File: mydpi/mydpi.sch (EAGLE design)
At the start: 16 parts, among them Q1 DMN3404L, U1 MEGA32U4-MU, U2 AP7381-33Y-13

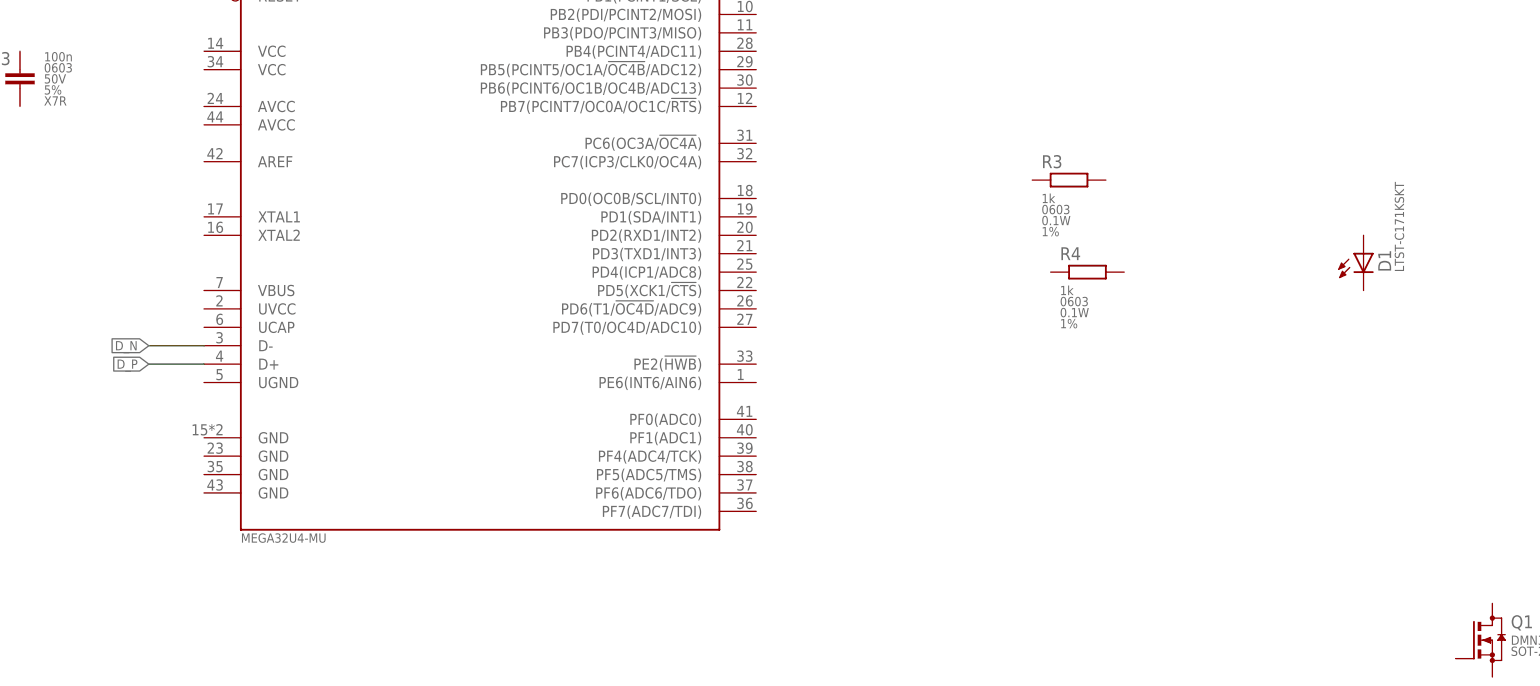
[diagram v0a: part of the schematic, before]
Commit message: Added supply voltage
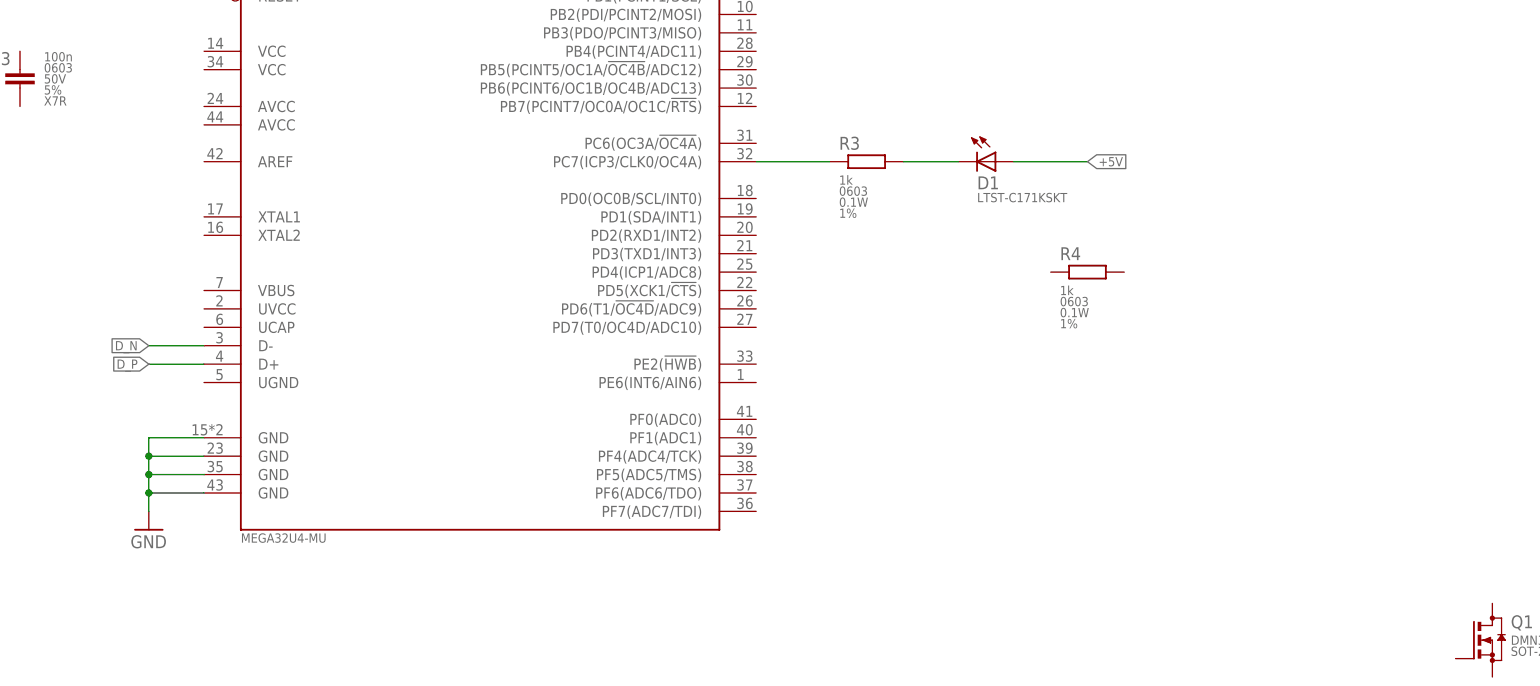
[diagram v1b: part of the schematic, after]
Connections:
- new net +5V: D1.A
- new net GND: U1.GND@1, U1.GND@2, U1.GND@3, U1.GND@4
- new net N$1: R3.1, U1.PC7(ICP3/CLK0/OC4A)
- new net N$2: D1.C, R3.2
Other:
- moved on the sheet: D1, R3
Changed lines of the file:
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@@
 <part name="Q1" library="zaan-Discrete" deviceset="DMN3404L" device="" package3d_urn="urn:adsk.eagle:package:28738/2"/>
 <part name="U2" library="zaan-IC-Power" deviceset="AP7381" device="-33Y-13"/>
+<part name="GND1" library="supply1" library_urn="urn:adsk.eagle:library:371" deviceset="GND" device=""/>
 </parts>
 <sheets>
@@
 <attribute name="DIELECTRIC" x="206.502" y="173.482" size="1.27" layer="96" align="center-left"/>
 </instance>
-<instance part="R3" gate="G$1" x="218.44" y="139.7" smashed="yes">
-<attribute name="NAME" x="214.63" y="142.24" size="1.778" layer="95" align="center-left"/>
-<attribute name="VALUE" x="214.63" y="137.16" size="1.27" layer="96" align="center-left"/>
-<attribute name="PACKAGE-IN" x="214.63" y="135.636" size="1.27" layer="96" align="center-left"/>
-<attribute name="POWER" x="214.63" y="134.112" size="1.27" layer="96" align="center-left"/>
-<attribute name="TOLERANCE" x="214.63" y="132.588" size="1.27" layer="96" align="center-left"/>
+<instance part="R3" gate="G$1" x="190.5" y="142.24" smashed="yes">
+<attribute name="NAME" x="186.69" y="144.78" size="1.778" layer="95" align="center-left"/>
+<attribute name="VALUE" x="186.69" y="139.7" size="1.27" layer="96" align="center-left"/>
+<attribute name="PACKAGE-IN" x="186.69" y="138.176" size="1.27" layer="96" align="center-left"/>
+<attribute name="POWER" x="186.69" y="136.652" size="1.27" layer="96" align="center-left"/>
+<attribute name="TOLERANCE" x="186.69" y="135.128" size="1.27" layer="96" align="center-left"/>
 </instance>
 <instance part="R4" gate="G$1" x="220.98" y="127" smashed="yes">
@@
 <attribute name="TOLERANCE" x="217.17" y="119.888" size="1.27" layer="96" align="center-left"/>
 </instance>
-<instance part="D1" gate="G$1" x="259.08" y="129.54" smashed="yes">
-<attribute name="NAME" x="262.89" y="127" size="1.778" layer="95" rot="R90"/>
-<attribute name="VALUE" x="264.668" y="127" size="1.27" layer="96" rot="R90"/>
+<instance part="D1" gate="G$1" x="208.28" y="142.24" smashed="yes" rot="R270">
+<attribute name="NAME" x="205.74" y="138.43" size="1.778" layer="95"/>
+<attribute name="VALUE" x="205.74" y="136.652" size="1.27" layer="96"/>
 </instance>
 <instance part="Q1" gate="G$1" x="276.86" y="76.2" smashed="yes">
@@
 <attribute name="NAME" x="289.56" y="102.108" size="1.778" layer="95"/>
 <attribute name="VALUE" x="299.72" y="91.694" size="1.27" layer="96"/>
+</instance>
+<instance part="GND1" gate="1" x="91.44" y="91.44" smashed="yes">
+<attribute name="VALUE" x="88.9" y="88.9" size="1.778" layer="96"/>
 </instance>
 </instances>
@@
 <wire x1="99.06" y1="114.3" x2="91.44" y2="114.3" width="0.1524" layer="91"/>
 <label x="91.44" y="114.3" size="1.27" layer="95" rot="R180" xref="yes"/>
+</segment>
+</net>
+<net name="GND" class="0">
+<segment>
+<pinref part="U1" gate="G$1" pin="GND@1"/>
+<wire x1="99.06" y1="104.14" x2="91.44" y2="104.14" width="0.1524" layer="91"/>
+<wire x1="91.44" y1="104.14" x2="91.44" y2="101.6" width="0.1524" layer="91"/>
+<pinref part="U1" gate="G$1" pin="GND@2"/>
+<wire x1="91.44" y1="101.6" x2="91.44" y2="99.06" width="0.1524" layer="91"/>
+<wire x1="91.44" y1="99.06" x2="91.44" y2="96.52" width="0.1524" layer="91"/>
+<wire x1="91.44" y1="96.52" x2="91.44" y2="93.98" width="0.1524" layer="91"/>
+<wire x1="99.06" y1="101.6" x2="91.44" y2="101.6" width="0.1524" layer="91"/>
+<junction x="91.44" y="101.6"/>
+<pinref part="U1" gate="G$1" pin="GND@3"/>
+<wire x1="99.06" y1="99.06" x2="91.44" y2="99.06" width="0.1524" layer="91"/>
+<junction x="91.44" y="99.06"/>
+<pinref part="U1" gate="G$1" pin="GND@4"/>
+<wire x1="99.06" y1="96.52" x2="91.44" y2="96.52" width="0.1524" layer="91"/>
+<junction x="91.44" y="96.52"/>
+<pinref part="GND1" gate="1" pin="GND"/>
+</segment>
+</net>
+<net name="N$1" class="0">
+<segment>
+<pinref part="U1" gate="G$1" pin="PC7(ICP3/CLK0/OC4A)"/>
+<wire x1="175.26" y1="142.24" x2="185.42" y2="142.24" width="0.1524" layer="91"/>
+<pinref part="R3" gate="G$1" pin="1"/>
+</segment>
+</net>
+<net name="N$2" class="0">
+<segment>
+<pinref part="R3" gate="G$1" pin="2"/>
+<pinref part="D1" gate="G$1" pin="C"/>
+<wire x1="195.58" y1="142.24" x2="203.2" y2="142.24" width="0.1524" layer="91"/>
+</segment>
+</net>
+<net name="+5V" class="0">
+<segment>
+<pinref part="D1" gate="G$1" pin="A"/>
+<wire x1="210.82" y1="142.24" x2="220.98" y2="142.24" width="0.1524" layer="91"/>
+<label x="220.98" y="142.24" size="1.27" layer="95" xref="yes"/>
 </segment>
 </net>
@@
 </drawing>
 <compatibility>
+<note version="8.2" severity="warning">
+Since Version 8.2, EAGLE supports online libraries. The ids
+of those online libraries will not be understood (or retained)
+with this version.
+</note>
 <note version="8.3" severity="warning">
 Since Version 8.3, EAGLE supports URNs for individual library

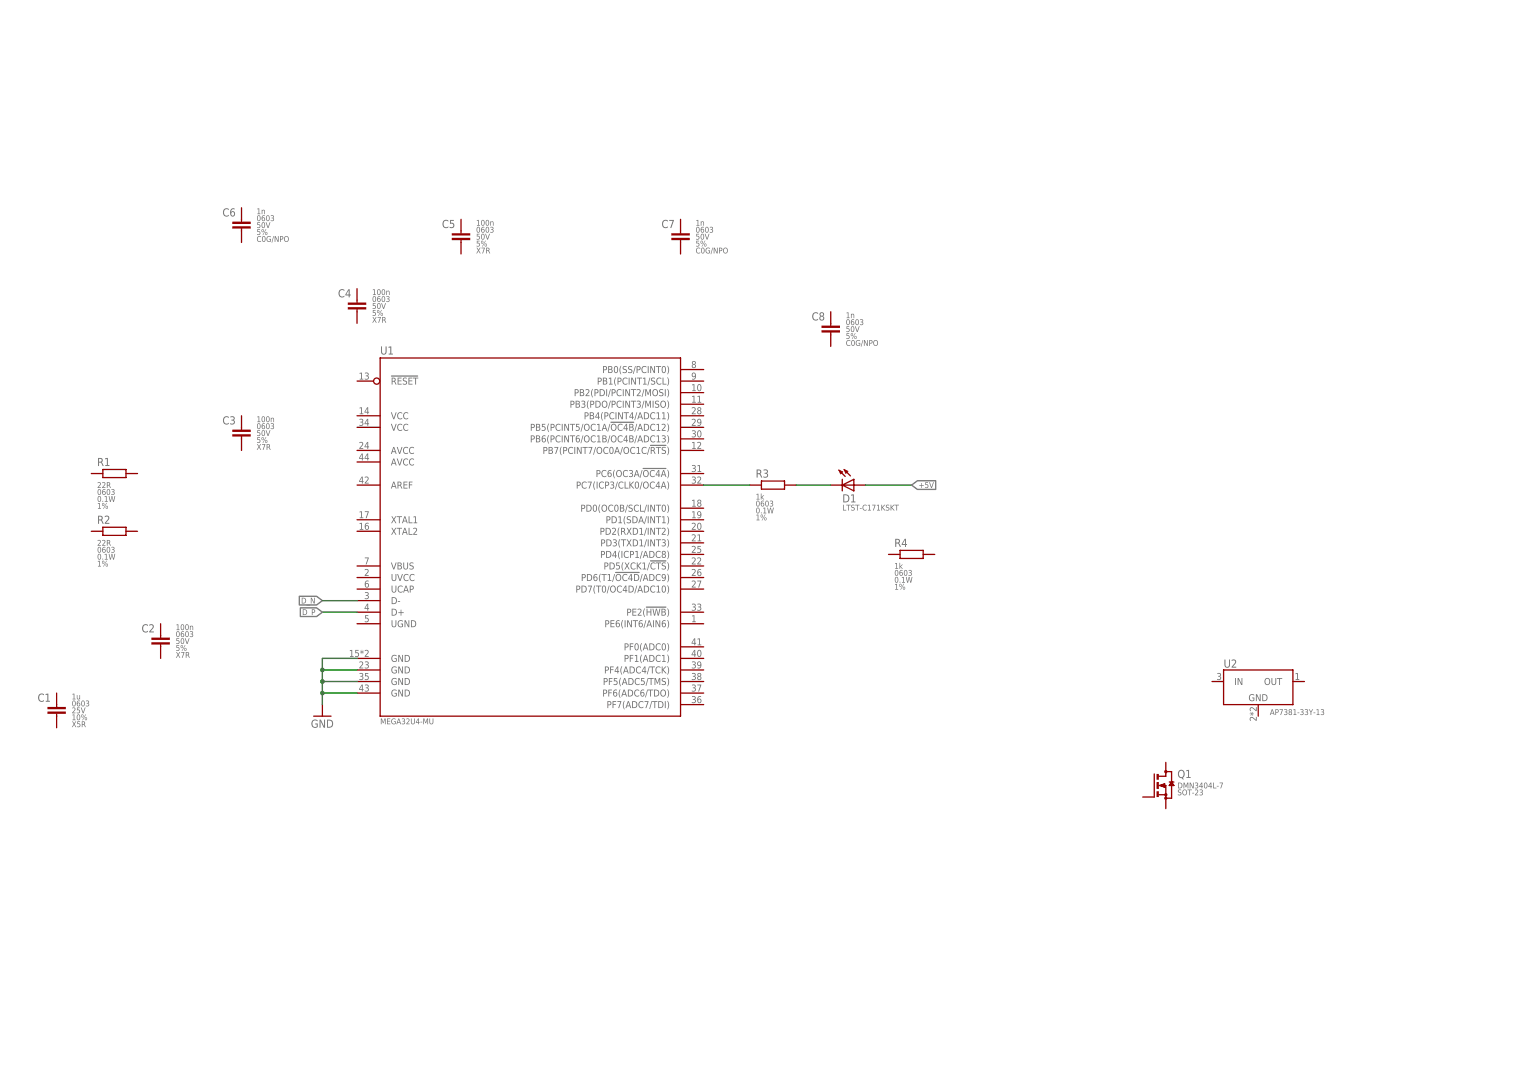
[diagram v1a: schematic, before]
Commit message: CC resistors added
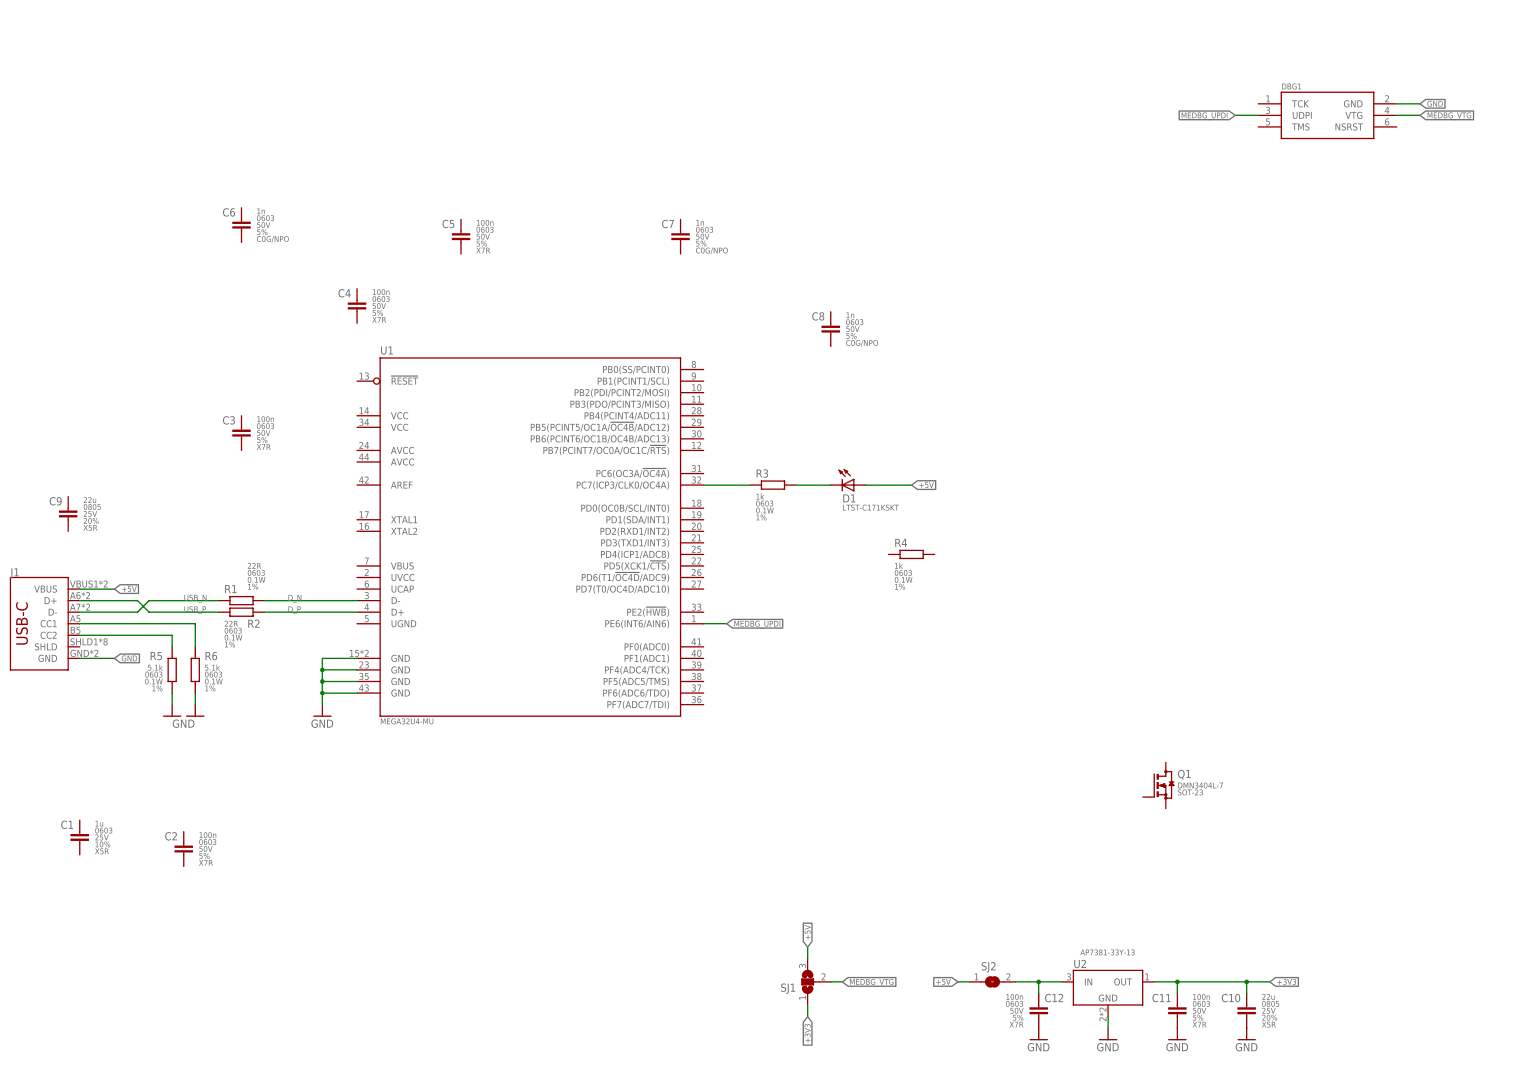
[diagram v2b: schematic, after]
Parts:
- added C10, C9: 22u, zaan-Capacitors:22UF-0805-25V-20%
- added C11, C12: 100n, zaan-Capacitors:100NF-0603-50V-5%
- added DBG1: AVR-UPDI-SKEDD, zaan-Connectors:AVR-UPDI-SKEDD
- added J1: (no value), zaan-Connectors:USB_C2-LAYER
- added R5, R6: 5.1k, zaan-Resistors:5.1KOHM-0603-1/10W-1%
- added SJ1: (no value), jumper:SJ2W
- added SJ2: (no value), jumper:SJ
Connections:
- new net +3V3: C10.1, C11.1, SJ1.1, U2.OUT
- new net MEDBG_UPDI: DBG1.UDPI, U1.PE6(INT6/AIN6)
- new net MEDBG_VTG: DBG1.VTG, SJ1.2
- new net N$4: C12.1, SJ2.2, U2.IN
- new net N$5: J1.CC2, R5.2
- new net N$6: J1.CC1, R6.2
- new net USB_N: J1.D-, R1.1
- new net USB_P: J1.D+, R2.1
- net +5V: now also J1.VBUS, SJ1.3, SJ2.1
- net D_N: now also R1.2
- net D_P: now also R2.2
- net GND: now also C10.2, C11.2, C12.2, DBG1.GND, J1.GND, R5.1, R6.1, U2.GND
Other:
- moved on the sheet: C1, C2, R1, R2, U2

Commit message: Placement LDO, Caps
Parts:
- removed C8: 1n, zaan-Capacitors:1NF-0603-50V-5%
- removed R4: 1k, zaan-Resistors:1KOHM-0603-1/10W-1%
- removed SJ2: (no value), jumper:SJ
- added C13: 100n, zaan-Capacitors:100NF-0603-50V-5%
- added D2: LTST-C171KSKT, zaan-Optoelectronics:LTST-C171KSKT
- added ICSP1: AVR-ISP-1.27MM, zaan-Connectors:AVR-ISP-1.27MM
- added R7, R8: 100k, zaan-Resistors:100KOHM-0603-1/10W-1%
- added R9: 1k, zaan-Resistors:1KOHM-0603-1/10W-1%
- C6: value 1n -> 100n; device zaan-Capacitors:1NF-0603-50V-5% -> zaan-Capacitors:100NF-0603-50V-5%
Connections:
- removed net N$4: C12.1, SJ2.2, U2.IN
- new net N$13: U1.XTAL1
- new net N$14: U1.XTAL2
- new net N$7: R7.1, U1.PE2(!HWB!)
- new net N$8: C1.1, U1.UCAP
- new net N$9: D2.A, R9.2
- new net PDI: ICSP1.MOSI, U1.PB2(PDI/PCINT2/MOSI)
- new net PDO: ICSP1.MISO, U1.PB3(PDO/PCINT3/MISO)
- new net RST: C13.1, ICSP1.RST, R8.1, U1.!RESET!
- new net SCK: ICSP1.SCK, U1.PB1(PCINT1/SCL)
- net +5V: now also C12.1, C2.1, C3.1, C4.1, C5.1, C6.1, C7.1, ICSP1.VCC, R7.2, R8.2, R9.1, U1.AREF, U1.AVCC@1, U1.AVCC@2, U1.UVCC, U1.VBUS, U1.VCC@1, U1.VCC@2, U2.IN; no longer SJ2.1
- net D_N: now also R2.2; no longer R1.2
- net D_P: now also R1.2; no longer R2.2
- net GND: now also C1.2, C13.2, C2.2, C3.2, C4.2, C5.2, C6.2, C7.2, D2.C, ICSP1.GND, U1.UGND
- net USB_N: now also R2.1; no longer R1.1
- net USB_P: now also R1.1; no longer R2.1
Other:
- moved on the sheet: C1, C2, C3, C4, C5, C6, C7, C9, D1, DBG1, J1, R1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
